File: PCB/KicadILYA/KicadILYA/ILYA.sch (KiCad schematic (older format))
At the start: 6 parts, among them U1 NodeMCU1.0(ESP-12E), U101 Temperature_connector, U102 Pin-SocketESP8266_1x15_2, U103 Pin-SocketESP8266_1x15, U2 Relay_2_pins, U3101 Flow_connector

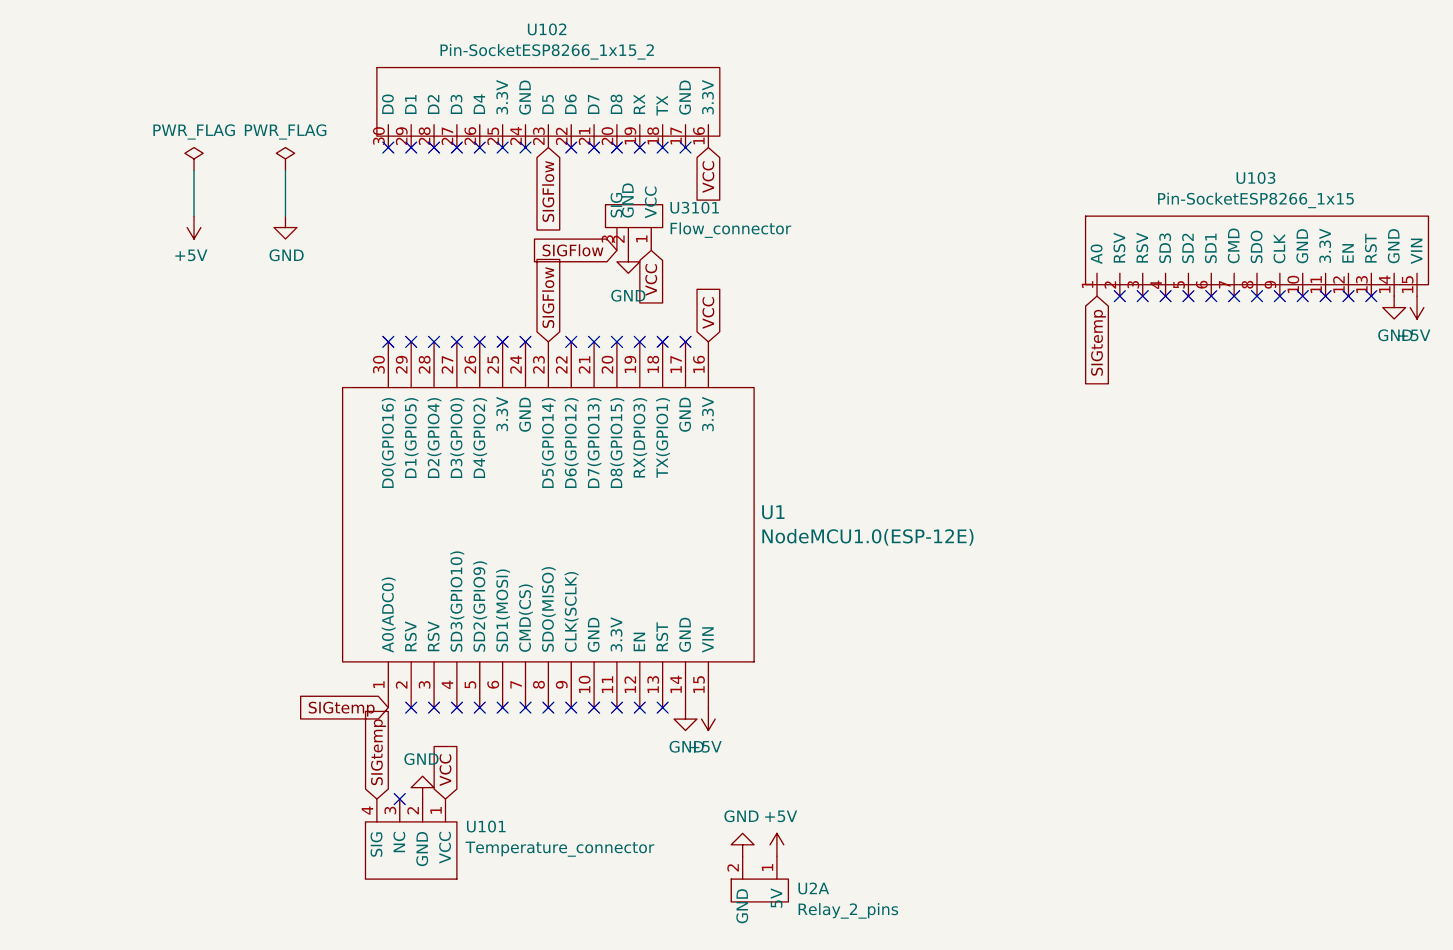
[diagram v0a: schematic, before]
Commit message: Correction of tracks size
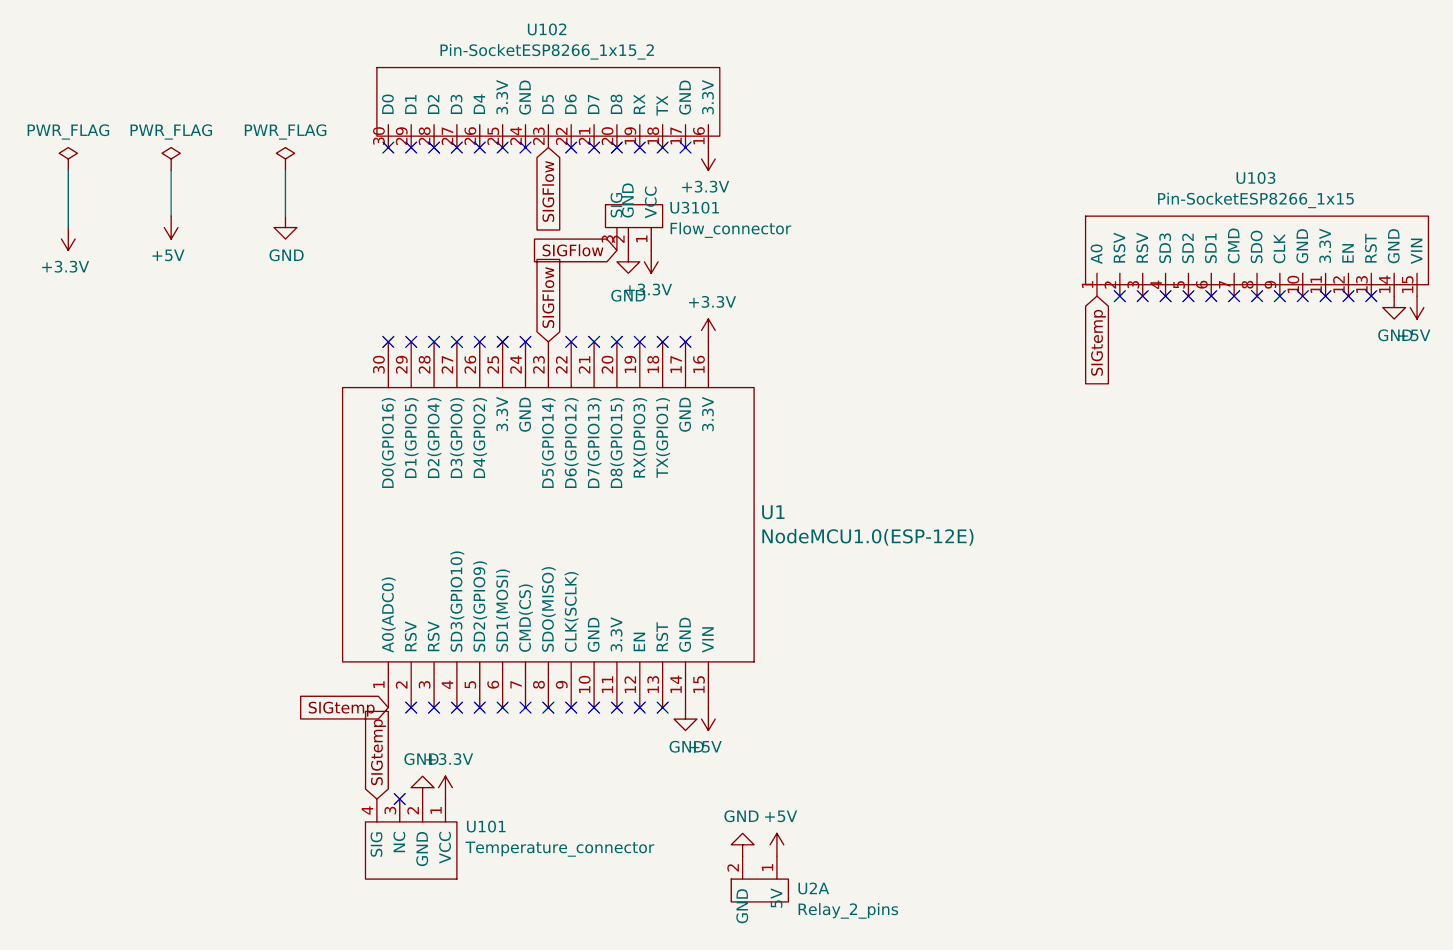
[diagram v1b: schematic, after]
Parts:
- U1: footprint wemos-d1-mini:SEEED_113990105_withoutPin -> nodemcu:SEEED_113990105
- U101: footprint pinHeads:PinHeader_1x04_P2.54mm_Horizontal -> Connector_PinHeader_2.54mm:PinHeader_1x04_P2.54mm_Horizontal
- U102: footprint pinSocket:PinSocket_1x15_P2.54mm_Vertical2 -> Connector_PinSocket_2.54mm:PinSocket_1x15_P2.54mm_Vertical2
- U103: footprint pinSocket:PinSocket_1x15_P2.54mm_Vertical -> Connector_PinSocket_2.54mm:PinSocket_1x15_P2.54mm_Vertical
- U2: footprint pinHeads:PinHeader_1x02_P2.54mm_Horizontal -> Connector_PinHeader_2.54mm:PinHeader_1x02_P2.54mm_Horizontal
- U3101: footprint pinHeads:PinHeader_1x03_P2.54mm_Horizontal -> Connector_PinSocket_2.54mm:PinSocket_1x03_P2.54mm_Horizontal
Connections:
- net VCC renamed +3V3
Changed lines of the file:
@@
 encoding utf-8
 Sheet 1 1
-Title ""
+Title "SHEILD for ESP8266"
 Date ""
 Rev ""
-Comp ""
-Comment1 ""
+Comp "INSA"
+Comment1 "Vincent Laurens"
 Comment2 ""
 Comment3 ""
@@
 F 0 "U2" H 5562 4293 50  0000 R CNN
 F 1 "Relay_2_pins" H 5562 4384 50  0000 R CNN
-F 2 "pinHeads:PinHeader_1x02_P2.54mm_Horizontal" H 5600 4600 50  0001 C CNN
+F 2 "Connector_PinHeader_2.54mm:PinHeader_1x02_P2.54mm_Horizontal" H 5600 4600 50  0001 C CNN
 F 3 "" H 5600 4600 50  0001 C CNN
 	1    5600 4600
@@
 F 0 "U3101" H 5078 885 50  0000 L CNN
 F 1 "Flow_connector" H 5078 794 50  0000 L CNN
-F 2 "pinHeads:PinHeader_1x03_P2.54mm_Horizontal" H 5000 1100 50  0001 C CNN
+F 2 "Connector_PinSocket_2.54mm:PinSocket_1x03_P2.54mm_Horizontal" H 5000 1100 50  0001 C CNN
 F 3 "" H 5000 1100 50  0001 C CNN
 	1    5000 1100
@@
 F 0 "U101" H 3412 4022 50  0000 R CNN
 F 1 "Temperature_connector" H 3412 4113 50  0000 R CNN
-F 2 "pinHeads:PinHeader_1x04_P2.54mm_Horizontal" H 3800 4300 50  0001 C CNN
+F 2 "Connector_PinHeader_2.54mm:PinHeader_1x04_P2.54mm_Horizontal" H 3800 4300 50  0001 C CNN
 F 3 "" H 3800 4300 50  0001 C CNN
 	1    3800 4300
@@
 L power:+5V #PWR0101
 U 1 1 5DFBDC88
-P 3000 1350
-F 0 "#PWR0101" H 3000 1200 50  0001 C CNN
-F 1 "+5V" H 3015 1523 50  0000 C CNN
-F 2 "" H 3000 1350 50  0001 C CNN
-F 3 "" H 3000 1350 50  0001 C CNN
-	1    3000 1350
+P 2900 1350
+F 0 "#PWR0101" H 2900 1200 50  0001 C CNN
+F 1 "+5V" H 2915 1523 50  0000 C CNN
+F 2 "" H 2900 1350 50  0001 C CNN
+F 3 "" H 2900 1350 50  0001 C CNN
+	1    2900 1350
 	-1   0    0    1
 $EndComp
@@
 L power:PWR_FLAG #FLG0101
 U 1 1 5DFBE05D
-P 3000 1150
-F 0 "#FLG0101" H 3000 1225 50  0001 C CNN
-F 1 "PWR_FLAG" H 3000 1324 50  0000 C CNN
-F 2 "" H 3000 1150 50  0001 C CNN
-F 3 "~" H 3000 1150 50  0001 C CNN
-	1    3000 1150
+P 2900 1150
+F 0 "#FLG0101" H 2900 1225 50  0001 C CNN
+F 1 "PWR_FLAG" H 2900 1324 50  0000 C CNN
+F 2 "" H 2900 1150 50  0001 C CNN
+F 3 "~" H 2900 1150 50  0001 C CNN
+	1    2900 1150
 	1    0    0    -1
 $EndComp
 Wire Wire Line
-	3000 1150 3000 1350
-Text GLabel 5250 1900 1    50   Input ~ 0
-VCC
-Text GLabel 5000 1500 3    50   Input ~ 0
-VCC
+	2900 1150 2900 1350
 NoConn ~ 3950 3500
 NoConn ~ 3900 3900
@@
 	-1   0    0    1
 $EndComp
-Text GLabel 4100 3900 1    50   Input ~ 0
-VCC
 $Comp
 L power:GND #PWR0110
@@
 F 0 "U1" V 4603 1772 60  0000 R CNN
 F 1 "NodeMCU1.0(ESP-12E)" V 4497 1772 60  0000 R CNN
-F 2 "wemos-d1-mini:SEEED_113990105_withoutPin" H 3950 1850 60  0001 C CNN
+F 2 "nodemcu:SEEED_113990105" H 3950 1850 60  0001 C CNN
 F 3 "" H 3950 1850 60  0000 C CNN
 	1    4550 2700
@@
 NoConn ~ 8050 1700
 NoConn ~ 8150 1700
-Text GLabel 5250 1050 3    50   Input ~ 0
-VCC
 $Comp
 L power:GND #PWR0108
@@
 F 0 "U102" H 4545 1765 50  0000 C CNN
 F 1 "Pin-SocketESP8266_1x15_2" H 4545 1674 50  0000 C CNN
-F 2 "pinSocket:PinSocket_1x15_P2.54mm_Vertical2" H 4800 1150 50  0001 C CNN
+F 2 "Connector_PinSocket_2.54mm:PinSocket_1x15_P2.54mm_Vertical2" H 4800 1150 50  0001 C CNN
 F 3 "" H 4800 1150 50  0001 C CNN
 	1    4800 1150
@@
 F 0 "U103" H 7645 1015 50  0000 C CNN
 F 1 "Pin-SocketESP8266_1x15" H 7645 924 50  0000 C CNN
-F 2 "pinSocket:PinSocket_1x15_P2.54mm_Vertical" H 8000 1100 50  0001 C CNN
+F 2 "Connector_PinSocket_2.54mm:PinSocket_1x15_P2.54mm_Vertical" H 8000 1100 50  0001 C CNN
 F 3 "" H 8000 1100 50  0001 C CNN
 	1    8000 1100
 	1    0    0    -1
 $EndComp
+$Comp
+L power:+3.3V #PWR0111
+U 1 1 5DFFBA8E
+P 2450 1400
+F 0 "#PWR0111" H 2450 1250 50  0001 C CNN
+F 1 "+3.3V" H 2465 1573 50  0000 C CNN
+F 2 "" H 2450 1400 50  0001 C CNN
+F 3 "" H 2450 1400 50  0001 C CNN
+	1    2450 1400
+	-1   0    0    1
+$EndComp
+$Comp
+L power:PWR_FLAG #FLG0103
+U 1 1 5DFFBAB8
+P 2450 1150
+F 0 "#FLG0103" H 2450 1225 50  0001 C CNN
+F 1 "PWR_FLAG" H 2450 1324 50  0000 C CNN
+F 2 "" H 2450 1150 50  0001 C CNN
+F 3 "~" H 2450 1150 50  0001 C CNN
+	1    2450 1150
+	1    0    0    -1
+$EndComp
+Wire Wire Line
+	2450 1150 2450 1400
+$Comp
+L power:+3.3V #PWR0114
+U 1 1 5DFFBBCD
+P 5250 1050
+F 0 "#PWR0114" H 5250 900 50  0001 C CNN
+F 1 "+3.3V" H 5265 1223 50  0000 C CNN
+F 2 "" H 5250 1050 50  0001 C CNN
+F 3 "" H 5250 1050 50  0001 C CNN
+	1    5250 1050
+	-1   0    0    1
+$EndComp
+$Comp
+L power:+3.3V #PWR0113
+U 1 1 5DFFBBFE
+P 5000 1500
+F 0 "#PWR0113" H 5000 1350 50  0001 C CNN
+F 1 "+3.3V" H 5015 1673 50  0000 C CNN
+F 2 "" H 5000 1500 50  0001 C CNN
+F 3 "" H 5000 1500 50  0001 C CNN
+	1    5000 1500
+	-1   0    0    1
+$EndComp
+$Comp
+L power:+3.3V #PWR0115
+U 1 1 5DFFBC1B
+P 5250 1900
+F 0 "#PWR0115" H 5250 1750 50  0001 C CNN
+F 1 "+3.3V" H 5265 2073 50  0000 C CNN
+F 2 "" H 5250 1900 50  0001 C CNN
+F 3 "" H 5250 1900 50  0001 C CNN
+	1    5250 1900
+	1    0    0    -1
+$EndComp
+$Comp
+L power:+3.3V #PWR0112
+U 1 1 5DFFBDAC
+P 4100 3900
+F 0 "#PWR0112" H 4100 3750 50  0001 C CNN
+F 1 "+3.3V" H 4115 4073 50  0000 C CNN
+F 2 "" H 4100 3900 50  0001 C CNN
+F 3 "" H 4100 3900 50  0001 C CNN
+	1    4100 3900
+	1    0    0    -1
+$EndComp
